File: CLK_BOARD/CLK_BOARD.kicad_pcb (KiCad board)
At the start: 4 copper layers, 46.5 x 38.7 mm, 80 parts, among them J1 PWR, J2 OUT_50M_1, J3 OUT_50M_2, J4 OUT_50M_3, J5 CTRL, J6 OUT_100M_3, J7 OUT_100M_2, J8 OUT_100M_1, U1 TPS7A9101DSKR, U2 LMK00804BQWRGTRQ1, U3 LMK00804BQWRGTRQ1, U4 SN74LVC1G74DCUR, X1 TB612-100.0M

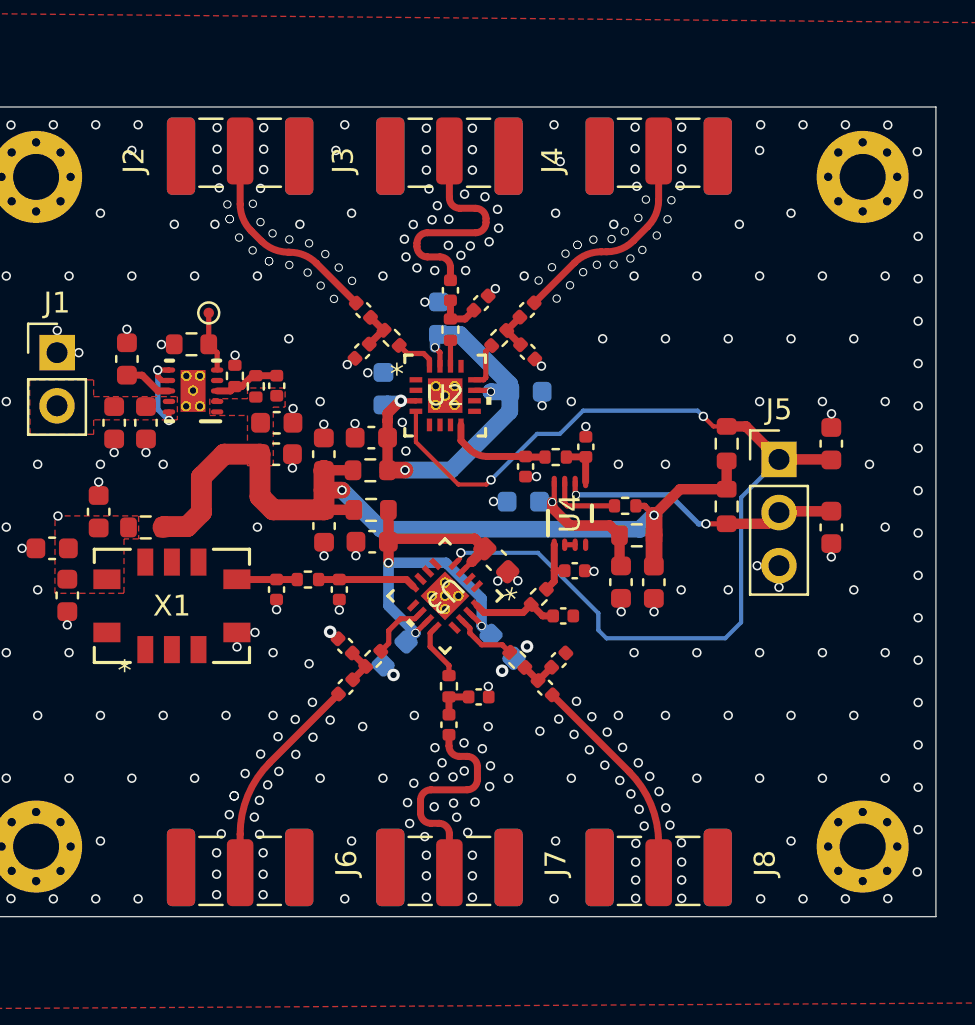
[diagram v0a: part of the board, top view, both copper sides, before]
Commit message: fixed some real issues, no DRC errors now
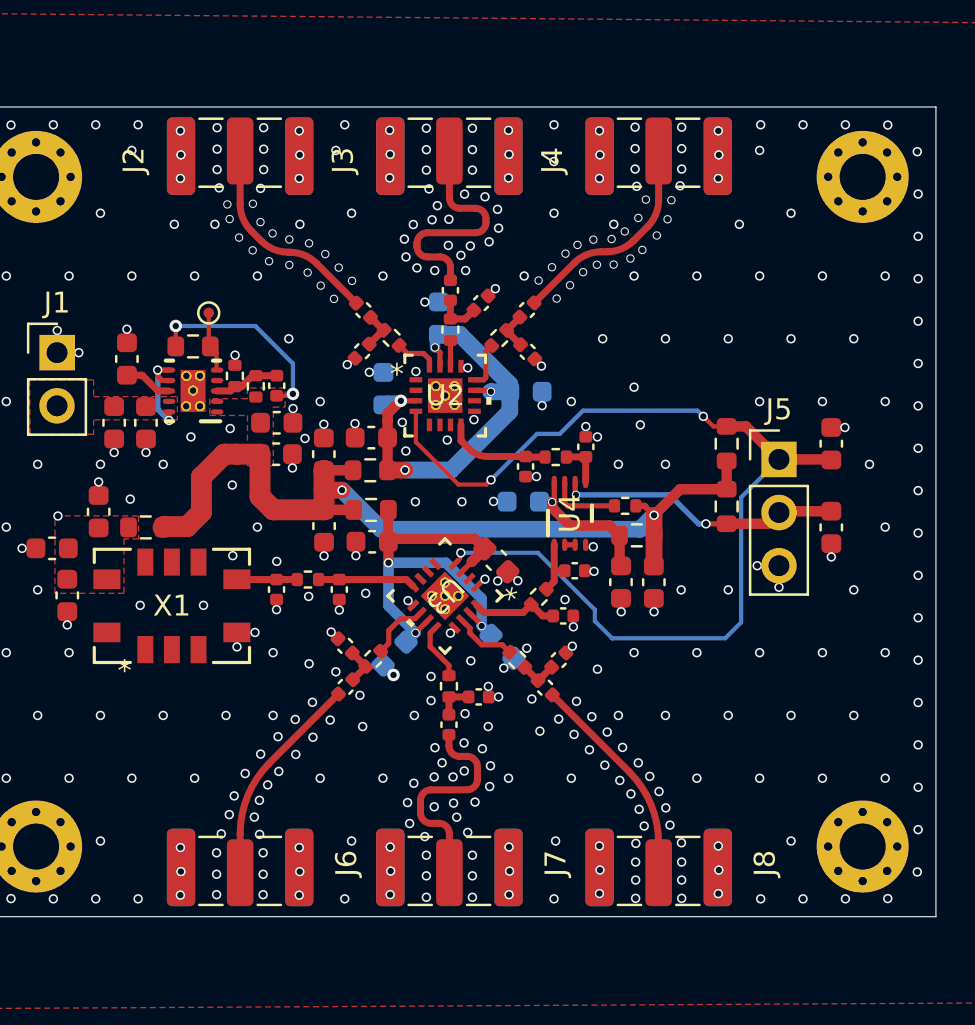
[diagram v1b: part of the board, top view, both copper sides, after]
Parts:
- moved R3 0.12 mm to (123.0, 72.1)
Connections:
- R3 pad 1: GND -> +3V3
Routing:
- net +3V3: track 42.8 -> 52.4 mm, vias 2 -> 4
- net GND: vias 342 -> 409

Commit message: fixed solder paste layers
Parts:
- added G***: LOGO, Snapeda:info_text, B.Cu at (135.2, 67.3)
